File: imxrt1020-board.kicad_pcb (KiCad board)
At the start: 2 copper layers, 102.9 x 68.6 mm, 191 parts, among them J1 Micro_SD_Card_Det, J10 CASTELATED, J11 CASTELATED, J12 CASTELATED, J13 CASTELATED, J14 CASTELATED, J15 CASTELATED, J16 CASTELATED, J17 CASTELATED, J18 CASTELATED, J19 CASTELATED, J2 USB_OTG, J20 CASTELATED, J21 CASTELATED, J22 CASTELATED, J23 CASTELATED, J24 CASTELATED, J25 CASTELATED, J26 CASTELATED, J27 CASTELATED, J28 CASTELATED, J29 CASTELATED, J3 Conn_02x20_Odd_Even, J30 CASTELATED, J31 CASTELATED, J32 CASTELATED, J33 CASTELATED, J34 CASTELATED, J35 CASTELATED, J36 CASTELATED, J37 CASTELATED, J38 CASTELATED, J39 CASTELATED, J4 CASTELATED, J40 CASTELATED, J41 CASTELATED, J42 CASTELATED, J43 CASTELATED, J44 GS2, J45 GS2, J46 PWR_IN, J47 JTAG, J48 Conn_01x06, J49 CASTELATED, J5 CASTELATED, J50 CASTELATED, J51 CASTELATED, J52 CASTELATED, J53 CASTELATED, J54 CASTELATED, J55 CASTELATED, J56 CASTELATED, J57 CASTELATED, J58 SI-50196-F, J59 CASTELATED, J6 CASTELATED, J60 CASTELATED, J61 CASTELATED, J62 CASTELATED, J63 CASTELATED, J64 CASTELATED, J65 CASTELATED, J66 CASTELATED, J67 CASTELATED, J68 CASTELATED, J7 CASTELATED, J8 CASTELATED, J9 CASTELATED, SW1 RST, SW2 SW_DIP_x02, SW3 WAKE, U1 imx_rt1020-qfp144, U2 M25PX32-VMW, U3 AS4C16M16S, U4 TPS3839DBZ, U5 LM1084-3.3, U6 ISL3178E, U7 KSZ8081RNA, U8 TCAN332D, U9 PRTR5V0U2X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

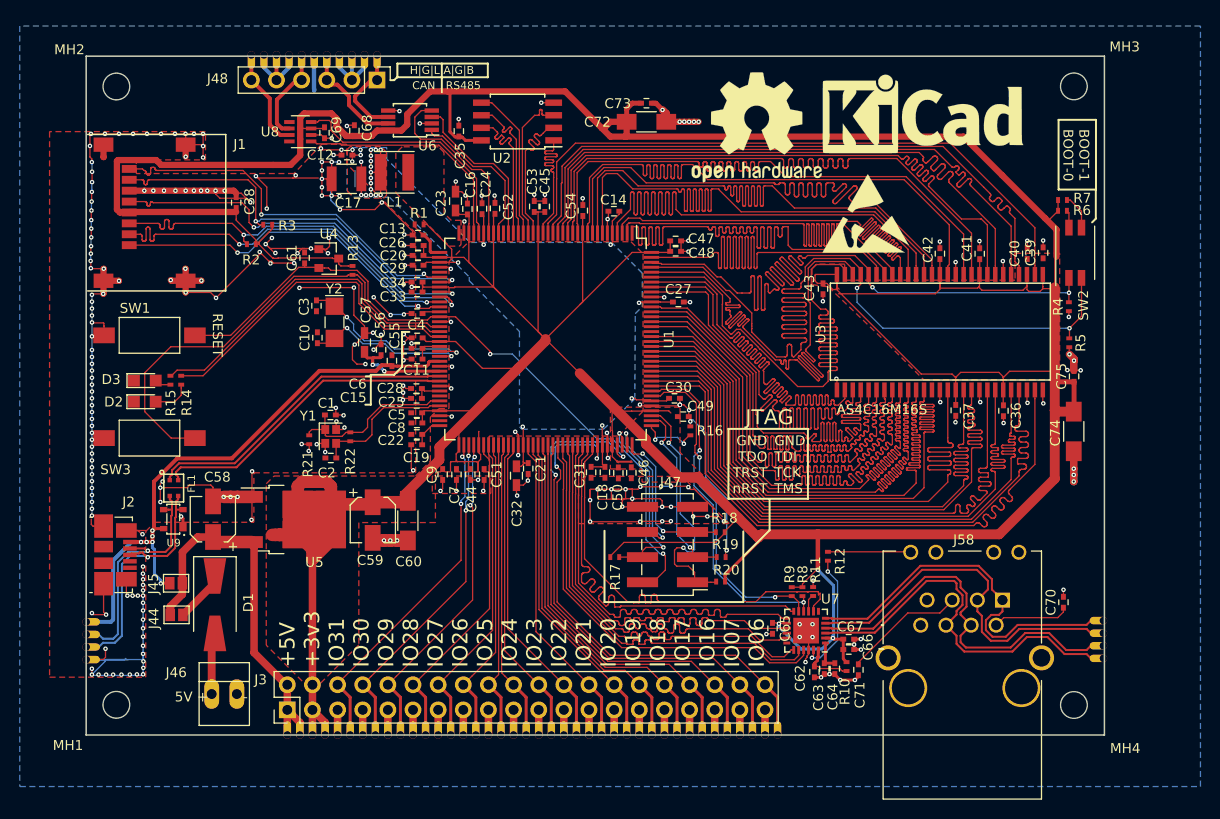
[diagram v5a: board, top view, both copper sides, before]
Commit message: Change USB protection, more silkscreen enances
Signed-off-by: Martin Ribelotta <martinribelotta@gmail.com>
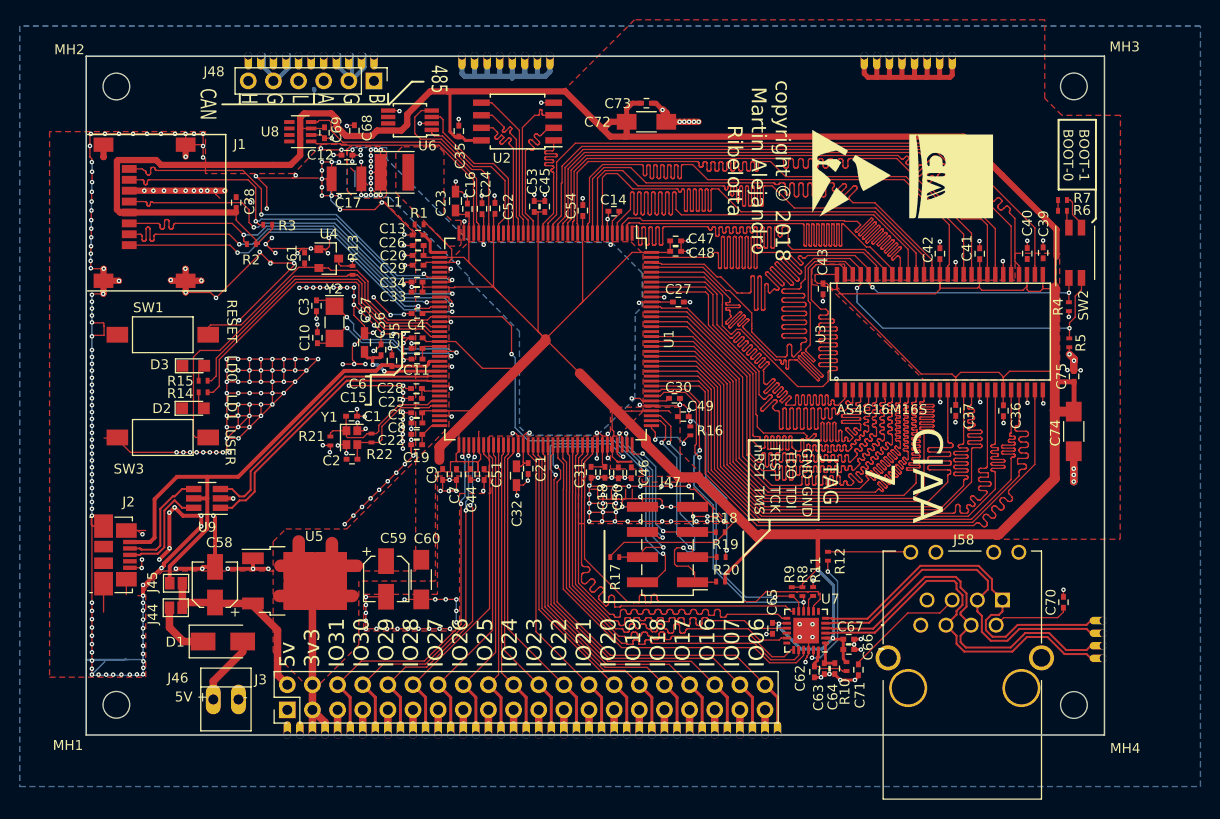
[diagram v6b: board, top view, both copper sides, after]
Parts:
- removed FL1: DLW21HN900SQ2L, local:SRF2012
- removed the REF*** at (192.3, 77.1)
- removed the REF*** at (175.5, 78.4)
- added G***: LOGO, local:LOGO-CIAA, F.Cu at (195.2, 83.4)
- added J69: CASTELATED, local:castelated_pad, F.Cu at (148.3, 71.2)
- added J70: CASTELATED, local:castelated_pad, F.Cu at (153.4, 71.2)
- added J71: CASTELATED, local:castelated_pad, F.Cu at (147.0, 71.2)
- added J72: CASTELATED, local:castelated_pad, F.Cu at (130.5, 71.2)
- added J73: CASTELATED, local:castelated_pad, F.Cu at (190.2, 71.2)
- added J74: CASTELATED, local:castelated_pad, F.Cu at (186.4, 71.2)
- added J75: CASTELATED, local:castelated_pad, F.Cu at (187.6, 71.2)
- added J76: CASTELATED, local:castelated_pad, F.Cu at (188.9, 71.2)
- added J77: CASTELATED, local:castelated_pad, F.Cu at (195.3, 71.2)
- added J78: CASTELATED, local:castelated_pad, F.Cu at (194.0, 71.2)
- added J79: CASTELATED, local:castelated_pad, F.Cu at (191.5, 71.2)
- added J80: CASTELATED, local:castelated_pad, F.Cu at (192.7, 71.2)
- D1: footprint Diodes_SMD:D_SMA-SMB_Universal_Handsoldering -> Diodes_SMD:D_SMA
- U9: value PRTR5V0U2X -> USBLC6-2; footprint local:SOT-143-4 -> TO_SOT_Packages_SMD:SOT-23-6_Handsoldering
- moved J65 72.4 mm to (152.1, 71.2), turned to 180 degrees
- moved J64 71.9 mm to (149.5, 71.2), turned to 180 degrees
- moved J63 70.8 mm to (145.7, 71.2), turned to 180 degrees
- moved J66 63.9 mm to (126.7, 71.2), turned to 180 degrees
- moved J68 18.7 mm to (154.6, 71.2)
- moved J67 16.2 mm to (150.8, 71.2)
- moved J50 8.58 mm to (134.3, 71.2)
- moved J53 7.31 mm to (135.6, 71.2)
- moved C58 6.62 mm to (120.8, 124.6)
- moved U5 6.20 mm to (128.8, 124.3)
- moved C59 6.10 mm to (138.1, 124.1)
- moved C60 6.10 mm to (141.6, 124.1)
- moved J56 5.39 mm to (128.0, 71.2)
- moved D3 5.12 mm to (118.6, 102.5)
- moved D2 4.91 mm to (118.6, 106.8)
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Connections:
- J63 pad 1: /GPIO/OTG_D+ -> GND
- J64 pad 1: /GPIO/OTG_D- -> GND
- J65 pad 1: /POWER/PWR_IN1 -> GND
- U9 pad 1: GND -> /GPIO/A_OTG_D+
- U9 pad 2: /GPIO/OTG_D+ -> GND
- U9 pad 3: /GPIO/OTG_D- -> /GPIO/A_OTG_D-
- U9 pad 4: /POWER/PWR_IN1 -> /GPIO/OTG_D-
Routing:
- net GND: track 507.9 -> 711.6 mm, vias 281 -> 407
- net +5V: track 41.4 -> 19.6 mm
- net /GPIO/OTG_D+: track 25.7 -> 11.2 mm, vias 1 -> 0
- net /GPIO/OTG_D-: track 24.9 -> 11.2 mm, vias 1 -> 0
- net (no net): track 0.00 -> 13.3 mm, vias 0 -> 4
- net /GPIO/RS485_B: track 11.1 -> 0.00 mm
- net /GPIO/CAN_H: track 10.2 -> 0.00 mm
- net /GPIO/RS485_A: track 9.93 -> 0.00 mm
- net /GPIO/CAN_L: track 9.74 -> 0.52 mm
- net +3V3: track 605.9 -> 613.8 mm, vias 3 -> 5
- net /POWER/PWR_IN1: track 61.8 -> 55.0 mm, vias 6 -> 0
- net /POWER/WAKEUP: track 47.3 -> 41.1 mm
- net /GPIO/JTAG_nRST: track 72.6 -> 77.3 mm
- net /GPIO/GPIO1_31: track 35.3 -> 39.1 mm
- net /GPIO/A_OTG_D-: track 32.1 -> 28.6 mm
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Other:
- board text added: "485"
- board text added: "5v 3v3 IO31 IO30 IO29 IO28 IO27 IO26 IO25 IO24 IO23 IO22 IO21 IO20 IO19 IO18 IO17 IO16 IO07 IO06"
- board text added: "B G A L G H"
- board text added: "CAN"
- board text added: "CIAA 7"
- board text added: "LD0"
- board text added: "LD1"
- board text added: "USER"
- board text added: "copyright © 2018 Martin Alejandro Ribelotta"
- board text removed: "+5V +3v3 IO31 IO30 IO29 IO28 IO27 IO26 IO25 IO24 IO23 IO22 IO21 IO20 IO19 IO18 IO17 IO16 IO07 IO06"
- board text removed: "CAN RS485"
- board text removed: "H|G|L|A|G|B"
